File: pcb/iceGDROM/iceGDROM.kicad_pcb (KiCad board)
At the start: 2 copper layers, 100 x 40 mm, 128 parts, among them J1 Micro_SD_Card_Det_Hirose_DM3AT, J2 Conn_02x22_Odd_Even, J3 Conn_02x04_Odd_Even, SW1 SW_Push, SW2 SW_Push, SW3 SW_Push, U1 ICE40HX8K-BG121, U2 LD1117S12TR_SOT223, U3 ME6206A25M3G_SOT23, U4 W25Q32JVSS, X1 SG-310SCF

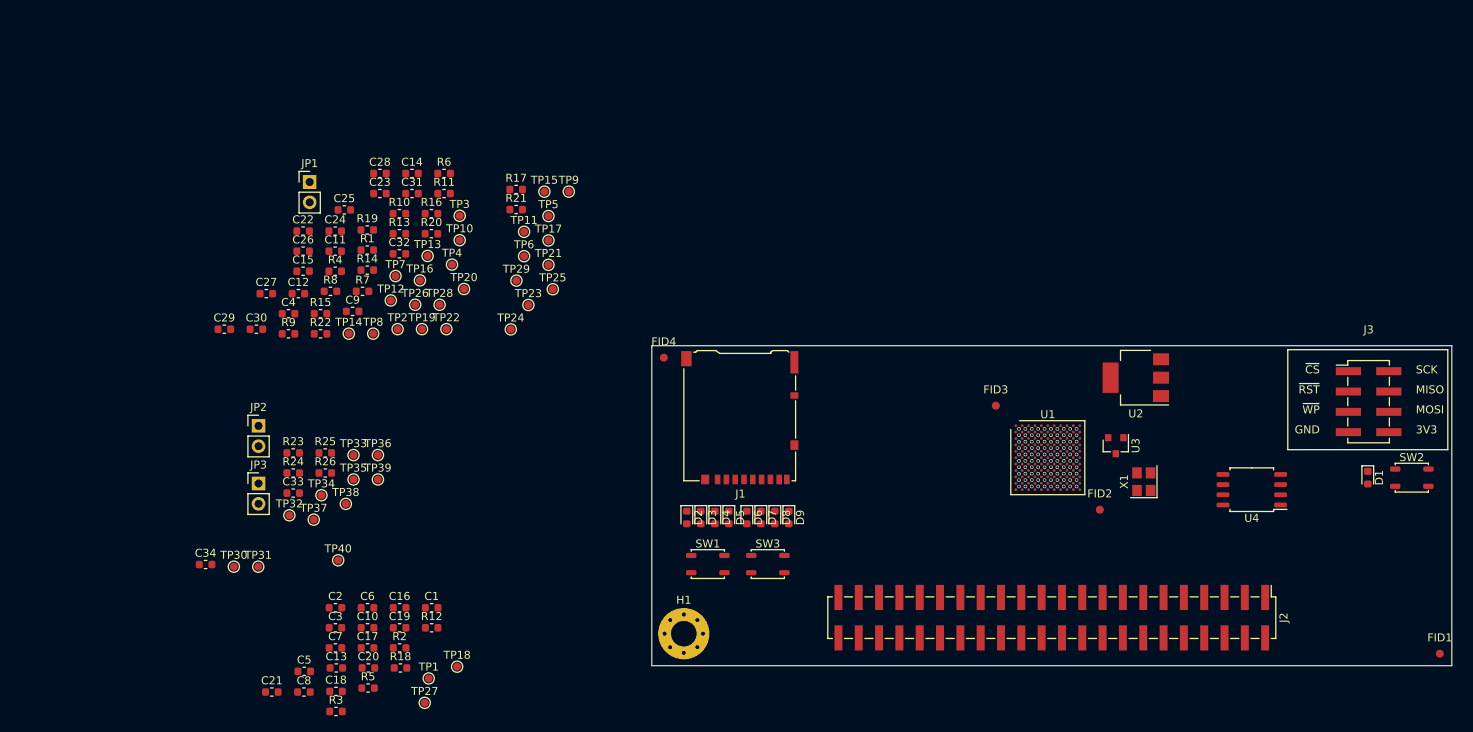
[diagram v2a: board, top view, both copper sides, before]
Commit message: Completed a functional version of the schematic and started with basic layout of the components on the PCB.
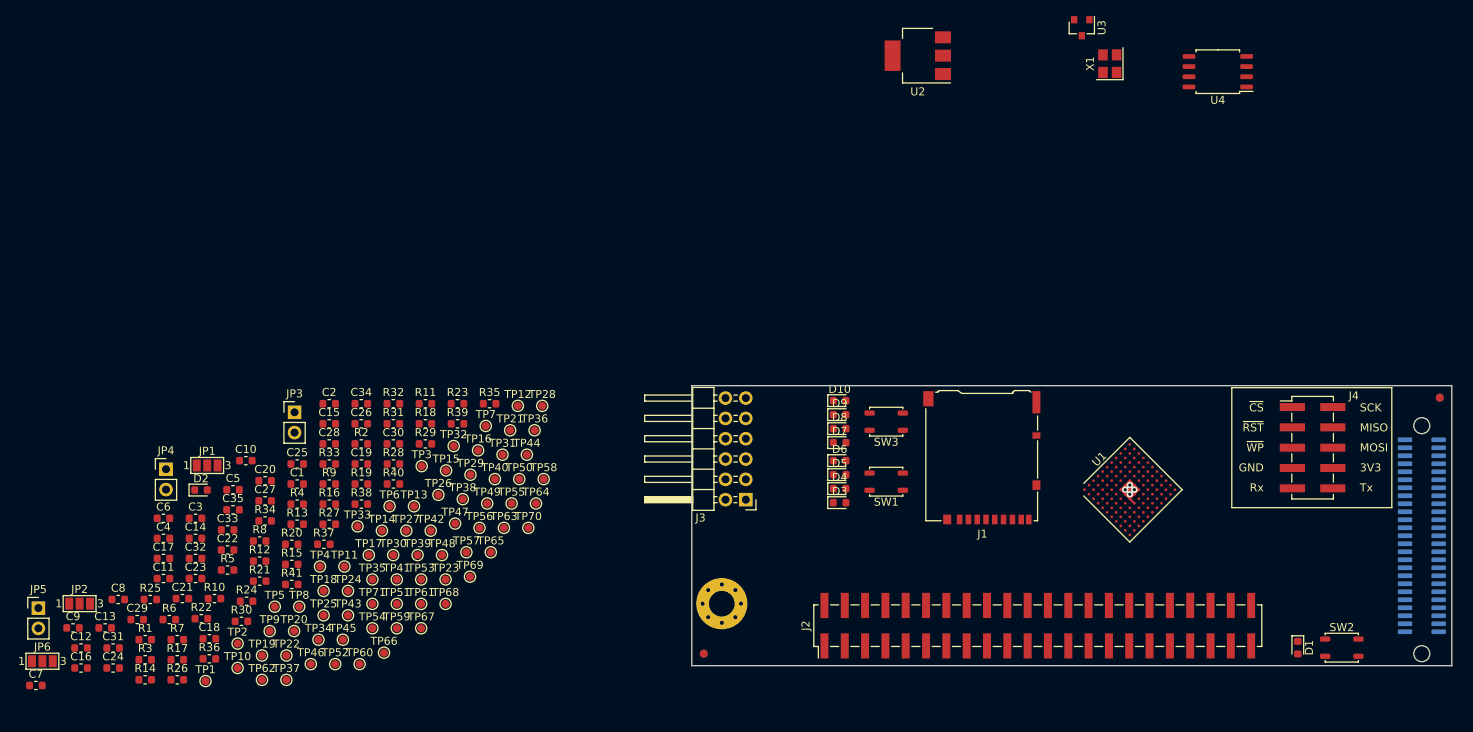
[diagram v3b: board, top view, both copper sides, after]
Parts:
- added C35: 10u, Capacitor_SMD:C_0603_1608Metric, F.Cu at (62.7, 85.5)
- added CN1: Molex_52602_0579, iceGDROM:Molex_052602_0579, B.Cu at (211.2, 89.2)
- added D2: LED, LED_SMD:LED_0603_1608Metric, F.Cu at (58.6, 83.0)
- added J4: Conn_02x05_Odd_Even, Connector_PinHeader_2.54mm:PinHeader_2x05_P2.54mm_Vertical_SMD, F.Cu at (197.6, 77.8)
- added JP4: Jumper_NC_Small, Connector_PinHeader_2.54mm:PinHeader_1x02_P2.54mm_Vertical, F.Cu at (54.3, 80.4)
- added JP5: Jumper_NC_Small, Connector_PinHeader_2.54mm:PinHeader_1x02_P2.54mm_Vertical, F.Cu at (38.3, 97.8)
- added JP6: Jumper_NC_Dual, Jumper:SolderJumper-3_P1.3mm_Open_Pad1.0x1.5mm_NumberLabels, F.Cu at (38.8, 104.4)
- added R27: 10K, Resistor_SMD:R_0603_1608Metric, F.Cu at (74.7, 87.3)
- added R28: 10K, Resistor_SMD:R_0603_1608Metric, F.Cu at (82.7, 79.8)
- added R29: 10K, Resistor_SMD:R_0603_1608Metric, F.Cu at (86.7, 77.3)
- added R30: 10K, Resistor_SMD:R_0603_1608Metric, F.Cu at (63.7, 99.5)
- added R31: 10K, Resistor_SMD:R_0603_1608Metric, F.Cu at (82.7, 74.8)
- added R32: 10K, Resistor_SMD:R_0603_1608Metric, F.Cu at (82.7, 72.3)
- added R33: 10K, Resistor_SMD:R_0603_1608Metric, F.Cu at (74.7, 79.8)
- added R34: 10K, Resistor_SMD:R_0603_1608Metric, F.Cu at (66.7, 86.9)
- added R35: 10K, Resistor_SMD:R_0603_1608Metric, F.Cu at (94.7, 72.3)
- added R36: NP, Resistor_SMD:R_0603_1608Metric, F.Cu at (59.7, 104.1)
- added R37: NP, Resistor_SMD:R_0603_1608Metric, F.Cu at (74.0, 89.8)
- added R38: 10K, Resistor_SMD:R_0603_1608Metric, F.Cu at (78.7, 84.8)
- added R39: 10K, Resistor_SMD:R_0603_1608Metric, F.Cu at (90.7, 74.8)
- added R40: 100R, Resistor_SMD:R_0603_1608Metric, F.Cu at (82.7, 82.3)
- added R41: 100R, Resistor_SMD:R_0603_1608Metric, F.Cu at (70.0, 94.8)
- added TP41: TestPoint_Probe, TestPoint:TestPoint_Pad_D1.0mm, F.Cu at (83.1, 94.2)
- added TP42: TestPoint_Probe, TestPoint:TestPoint_Pad_D1.0mm, F.Cu at (87.4, 88.1)
- added TP43: TestPoint_Probe, TestPoint:TestPoint_Pad_D1.0mm, F.Cu at (77.0, 98.7)
- added TP44: TestPoint_Probe, TestPoint:TestPoint_Pad_D1.0mm, F.Cu at (99.4, 78.6)
- added TP45: TestPoint_Probe, TestPoint:TestPoint_Pad_D1.0mm, F.Cu at (76.4, 101.8)
- added TP46: TestPoint_Probe, TestPoint:TestPoint_Pad_D1.0mm, F.Cu at (72.4, 104.8)
- added TP47: TestPoint_Probe, TestPoint:TestPoint_Pad_D1.0mm, F.Cu at (90.4, 87.2)
- added TP48: TestPoint_Probe, TestPoint:TestPoint_Pad_D1.0mm, F.Cu at (88.8, 91.2)
- added TP49: TestPoint_Probe, TestPoint:TestPoint_Pad_D1.0mm, F.Cu at (94.4, 84.7)
- added TP50: TestPoint_Probe, TestPoint:TestPoint_Pad_D1.0mm, F.Cu at (98.4, 81.7)
- added TP51: TestPoint_Probe, TestPoint:TestPoint_Pad_D1.0mm, F.Cu at (83.1, 97.3)
- added TP52: TestPoint_Probe, TestPoint:TestPoint_Pad_D1.0mm, F.Cu at (75.4, 104.8)
- added TP53: TestPoint_Probe, TestPoint:TestPoint_Pad_D1.0mm, F.Cu at (86.2, 94.2)
- added TP54: TestPoint_Probe, TestPoint:TestPoint_Pad_D1.0mm, F.Cu at (80.1, 100.3)
- added TP55: TestPoint_Probe, TestPoint:TestPoint_Pad_D1.0mm, F.Cu at (97.5, 84.7)
- added TP56: TestPoint_Probe, TestPoint:TestPoint_Pad_D1.0mm, F.Cu at (93.5, 87.8)
- added TP57: TestPoint_Probe, TestPoint:TestPoint_Pad_D1.0mm, F.Cu at (91.8, 90.8)
- added TP58: TestPoint_Probe, TestPoint:TestPoint_Pad_D1.0mm, F.Cu at (101.5, 81.7)
- added TP59: TestPoint_Probe, TestPoint:TestPoint_Pad_D1.0mm, F.Cu at (83.1, 100.3)
- added TP60: TestPoint_Probe, TestPoint:TestPoint_Pad_D1.0mm, F.Cu at (78.5, 104.8)
- added TP61: TestPoint_Probe, TestPoint:TestPoint_Pad_D1.0mm, F.Cu at (86.2, 97.3)
- added TP62: TestPoint_Probe, TestPoint:TestPoint_Pad_D1.0mm, F.Cu at (66.3, 106.8)
- added TP63: TestPoint_Probe, TestPoint:TestPoint_Pad_D1.0mm, F.Cu at (96.5, 87.8)
- added TP64: TestPoint, TestPoint:TestPoint_Pad_D1.0mm, F.Cu at (100.5, 84.7)
- added TP65: TestPoint, TestPoint:TestPoint_Pad_D1.0mm, F.Cu at (94.9, 90.8)
- added TP66: TestPoint, TestPoint:TestPoint_Pad_D1.0mm, F.Cu at (81.5, 103.4)
- added TP67: TestPoint, TestPoint:TestPoint_Pad_D1.0mm, F.Cu at (86.2, 100.3)
- added TP68: TestPoint, TestPoint:TestPoint_Pad_D1.0mm, F.Cu at (89.2, 97.3)
- added TP69: TestPoint, TestPoint:TestPoint_Pad_D1.0mm, F.Cu at (92.3, 93.9)
- added TP70: TestPoint, TestPoint:TestPoint_Pad_D1.0mm, F.Cu at (99.6, 87.8)
- added TP71: TestPoint, TestPoint:TestPoint_Pad_D1.0mm, F.Cu at (80.1, 97.3)
- C21: value 10n -> NP
- C22: value 100n -> 10n
- C30, C8: value 10u -> 100n
- C32, C9: value 100n -> 10u
- C33: value 1u0 -> 100n
- C34: value 10u -> 1u0
- FID3, FID4: moved to B.Cu
- J3: value Conn_02x04_Odd_Even -> PMOD; footprint Connector_PinHeader_2.54mm:PinHeader_2x04_P2.54mm_Vertical_SMD -> Connector_PinHeader_2.54mm:PinHeader_2x06_P2.54mm_Horizontal
- JP1, JP2: value Jumper_NC_Small -> Jumper_NC_Dual; footprint Connector_PinHeader_2.54mm:PinHeader_1x02_P2.54mm_Vertical -> Jumper:SolderJumper-3_P1.3mm_Open_Pad1.0x1.5mm_NumberLabels
- R10, R11: value 10K -> 1K
- R2: value R -> 100R
- R21, R22: value NP -> 10K
- R25, R26: value 100R -> 10K
- R3: value 1K -> 10K
- R4, R5, R6, R7: value 10K -> 100R
- R9: value 10K -> R
- TP1, TP10, TP11, TP12, TP13, TP14, TP15, TP16, TP17, TP18, TP19, TP2, TP20, TP21, TP22, TP23, TP24, TP25, TP26, TP27, TP28, TP29, TP3, TP30, TP31, TP36, TP37, TP38, TP39, TP4, TP5, TP6, TP7, TP8, TP9: value TestPoint -> TestPoint_Probe
- moved J3 78.8 mm to (126.8, 84.2), turned to 180 degrees
- moved R17 72.5 mm to (55.7, 104.3)
- moved C31 68.0 mm to (47.7, 102.8)
- moved TP9 66.4 mm to (67.2, 100.7)
- moved R6 65.5 mm to (54.7, 99.2)
- moved C24 61.3 mm to (47.7, 105.3)
- moved TP10 60.2 mm to (63.2, 105.3)
- moved TP5 59.6 mm to (67.9, 97.6)
- moved R14 58.3 mm to (51.7, 106.8)
- moved R21 56.4 mm to (66.0, 94.4)
- moved R1 56.1 mm to (51.7, 101.7)
- moved FID3 55.5 mm to (213.5, 71.5)
- moved R10 53.4 mm to (60.3, 96.6)
- moved C23 53.4 mm to (58.0, 94.1)
- moved C14 53.0 mm to (58.0, 89.1)
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- renumbered D9 to D10, D2 to D3, D3 to D4, D4 to D5, D5 to D6, D6 to D7, D7 to D8, D8 to D9
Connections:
- C10 pad 1: GND -> +3V3
- C10 pad 2: +3V3 -> GND
- C11 pad 1: +3V3 -> GND
- C11 pad 2: GND -> +3V3
- C12 pad 1: +3V3 -> GND
- C12 pad 2: GND -> +3V3
- C18 pad 1: Net-(C18-Pad1) -> /ROM_UP
- C21 pad 1: Net-(C21-Pad1) -> +3V3
- C22 pad 1: +3V3 -> /ROM_DWN
- C24 pad 1: +2V5 -> +3V3
- C25 pad 1: +1V2 -> +2V5
- C27 pad 1: Net-(C27-Pad1) -> +1V2
- C27 pad 2: Net-(C27-Pad2) -> GND
- C29 pad 1: +1V2 -> Net-(C29-Pad1)
- C29 pad 2: GND -> Net-(C29-Pad2)
- C30 pad 1: Net-(C27-Pad1) -> +1V2
- C30 pad 2: Net-(C27-Pad2) -> GND
- C32 pad 1: +1V2 -> Net-(C29-Pad1)
- C32 pad 2: GND -> Net-(C29-Pad2)
- C8 pad 1: GND -> +3V3
- C8 pad 2: +3V3 -> GND
- D10 pad 2: Net-(D9-Pad2) -> Net-(D10-Pad2)
- D3 pad 2: Net-(D2-Pad2) -> Net-(D3-Pad2)
- D4 pad 2: Net-(D3-Pad2) -> Net-(D4-Pad2)
- D5 pad 2: Net-(D4-Pad2) -> Net-(D5-Pad2)
- D6 pad 2: Net-(D5-Pad2) -> Net-(D6-Pad2)
- D7 pad 2: Net-(D6-Pad2) -> Net-(D7-Pad2)
- D8 pad 2: Net-(D7-Pad2) -> Net-(D8-Pad2)
- D9 pad 2: Net-(D8-Pad2) -> Net-(D9-Pad2)
- J3 pad 1: /FLASH_CSn -> Net-(J3-Pad1)
- J3 pad 2: /FPGA_SCK -> Net-(J3-Pad2)
- J3 pad 3: /FLASH_~RST~|IO3 -> Net-(J3-Pad3)
- J3 pad 4: /FLASH_MISO|IO1 -> Net-(J3-Pad4)
- J3 pad 5: /FLASH_~WP~|IO2 -> GND
- J3 pad 6: /FLASH_MOSI|IO0 -> +3V3
- J3 pad 7: GND -> Net-(J3-Pad7)
- J3 pad 8: +3V3 -> Net-(J3-Pad8)
- JP1 pad 1: /FLASH_CSn -> GND
- JP1 pad 2: Net-(JP1-Pad2) -> /CSEL
- JP2 pad 1: /FLASH_MOSI|IO0 -> +3V3
- JP2 pad 2: /FPGA_SDO -> /VLOGIC
- JP3 pad 1: /FPGA_SDI -> /FLASH_CSn
- JP3 pad 2: /FLASH_MISO|IO1 -> Net-(JP3-Pad2)
- R10 pad 1: Net-(D4-Pad2) -> Net-(R10-Pad1)
- R10 pad 2: /LED2 -> Net-(D1-Pad2)
- R11 pad 1: Net-(D5-Pad2) -> Net-(D2-Pad2)
- R11 pad 2: /LED3 -> +3V3
- R12 pad 1: Net-(C18-Pad1) -> GND
- R13 pad 1: GND -> Net-(J3-Pad1)
- R13 pad 2: Net-(R13-Pad2) -> /PMOD_1
- R14 pad 1: Net-(D6-Pad2) -> Net-(J3-Pad2)
- R14 pad 2: /LED4 -> /PMOD_2
- R15 pad 1: Net-(D7-Pad2) -> Net-(J3-Pad3)
- R15 pad 2: /LED5 -> /PMOD_3
- R16 pad 1: Net-(D8-Pad2) -> Net-(J3-Pad4)
- R16 pad 2: /LED6 -> /PMOD_4
- R17 pad 1: Net-(D9-Pad2) -> Net-(D3-Pad2)
- R17 pad 2: /LED7 -> /LED0
- R18 pad 1: Net-(C21-Pad1) -> Net-(D4-Pad2)
- R18 pad 2: Net-(R13-Pad2) -> /LED1
- R19 pad 1: +3V3 -> Net-(D5-Pad2)
- R19 pad 2: /FPGA_SCK -> /LED2
- R2 pad 1: Net-(R2-Pad1) -> /EMPH
- R2 pad 2: +3V3 -> /PB0
- R20 pad 1: +3V3 -> Net-(D6-Pad2)
- R20 pad 2: Net-(JP1-Pad2) -> /LED3
- R21 pad 1: +3V3 -> /ROM_UP
- R21 pad 2: /FLASH_MOSI|IO0 -> Net-(R12-Pad2)
- R22 pad 1: +3V3 -> Net-(C16-Pad2)
- R22 pad 2: /FLASH_MISO|IO1 -> Net-(R22-Pad2)
- R23 pad 1: +3V3 -> Net-(R22-Pad2)
- R23 pad 2: /FLASH_~WP~|IO2 -> +3V3
- R24 pad 1: +3V3 -> GND
- R24 pad 2: /FLASH_~RST~|IO3 -> Net-(R24-Pad2)
- R25 pad 1: +1V2 -> /PMOD_5
- R25 pad 2: Net-(C27-Pad1) -> Net-(J3-Pad7)
- R26 pad 1: +1V2 -> /PMOD_6
- R26 pad 2: Net-(C28-Pad1) -> Net-(J3-Pad8)
- R3 pad 1: Net-(R2-Pad1) -> GND
- R3 pad 2: Net-(D1-Pad2) -> /EMPH
- R4 pad 2: +3V3 -> /SDAT
- R5 pad 1: Net-(C16-Pad2) -> Net-(R5-Pad1)
- R5 pad 2: Net-(R5-Pad2) -> /SCK
- R6 pad 1: GND -> Net-(R6-Pad1)
- R6 pad 2: Net-(R12-Pad2) -> /CD_CLK
- R7 pad 1: Net-(R5-Pad2) -> Net-(R7-Pad1)
- R7 pad 2: +3V3 -> /LRCK
- R8 pad 1: Net-(D2-Pad2) -> Net-(R8-Pad1)
- R8 pad 2: /LED0 -> +3V3
- R9 pad 1: Net-(D3-Pad2) -> Net-(R10-Pad1)
- R9 pad 2: /LED1 -> +3V3
- SW2 pad 1: Net-(R5-Pad2) -> Net-(R22-Pad2)
- SW3 pad 2: Net-(R13-Pad2) -> Net-(R24-Pad2)
- TP1 pad 1: Net-(R2-Pad1) -> /PB0
- TP10 pad 1: /D8 -> /ROM_DWN
- TP11 pad 1: /D9 -> /LED0
- TP12 pad 1: /D10 -> /REFCLK
- TP13 pad 1: /D11 -> /LED1
- TP14 pad 1: /D12 -> /LED2
- TP15 pad 1: /D13 -> /LED3
- TP16 pad 1: /D14 -> /LED4
- TP17 pad 1: /D15 -> /LED5
- TP18 pad 1: /REFCLK -> /LED6
- TP19 pad 1: /PB0 -> /LED7
- TP2 pad 1: /D0 -> /PB1
- TP20 pad 1: /PB1 -> /UART_Tx
- TP21 pad 1: /PB2 -> /UART_Rx
- TP22 pad 1: /PB3 -> /EMPH
- TP23 pad 1: /PB4 -> /CS0n
- TP24 pad 1: /PB5 -> /CS1n
- TP25 pad 1: /PB6 -> /RDn
- TP26 pad 1: /PB7 -> /WRn
- TP27 pad 1: Net-(C16-Pad2) -> /DMACKn
- TP28 pad 1: +12V -> /DMARQ
- TP29 pad 1: +5V -> /IORDY
- TP3 pad 1: /D1 -> /PB2
- TP30 pad 1: +3V3 -> /INTRQ
- TP31 pad 1: +2V5 -> /G_RST
- TP32 pad 1: +1V2 -> Net-(R10-Pad1)
- TP33 pad 1: Net-(JP1-Pad2) -> /REFCLK
- TP34 pad 1: /FPGA_SCK -> +1V2
- TP35 pad 1: Net-(C27-Pad1) -> +2V5
- TP36 pad 1: Net-(C28-Pad1) -> /PMOD_1
- TP37 pad 1: /FLASH_MOSI|IO0 -> /PMOD_2
- TP38 pad 1: /FLASH_MISO|IO1 -> /PMOD_3
- TP39 pad 1: /FLASH_~WP~|IO2 -> /PMOD_4
- TP4 pad 1: /D2 -> /PB3
- TP40 pad 1: /FLASH_~RST~|IO3 -> Net-(C16-Pad2)
- TP5 pad 1: /D3 -> /PB4
- TP6 pad 1: /D4 -> /PB5
- TP7 pad 1: /D5 -> /PB6
- TP8 pad 1: /D6 -> /PB7
- TP9 pad 1: /D7 -> /ROM_UP
- U1 pad A10: Net-(U1-PadA10) -> /PB1
- U1 pad A11: Net-(U1-PadA11) -> /PB0
- U1 pad A2: Net-(U1-PadA2) -> /UART_Tx
- U1 pad A3: Net-(U1-PadA3) -> /UART_Rx
- U1 pad A4: Net-(U1-PadA4) -> /LED4
- U1 pad A5: Net-(U1-PadA5) -> /LED2
- U1 pad A6: Net-(U1-PadA6) -> /LED1
- U1 pad A7: Net-(U1-PadA7) -> /LED0
- U1 pad A8: Net-(U1-PadA8) -> /ROM_UP
- U1 pad A9: Net-(U1-PadA9) -> /PB5
- U1 pad B1: Net-(U1-PadB1) -> /D0
- U1 pad B2: Net-(U1-PadB2) -> /D1
- U1 pad B3: Net-(U1-PadB3) -> /LED7
- U1 pad B4: Net-(U1-PadB4) -> /LED6
- U1 pad B5: Net-(U1-PadB5) -> /LED3
- U1 pad B6: Net-(U1-PadB6) -> /REFCLK
- U1 pad B8: Net-(U1-PadB8) -> /PB4
- U1 pad B9: Net-(U1-PadB9) -> /PB3
- U1 pad C1: Net-(U1-PadC1) -> /D5
- U1 pad C2: Net-(U1-PadC2) -> /D4
- U1 pad C3: Net-(U1-PadC3) -> /D3
- U1 pad C4: Net-(U1-PadC4) -> /D2
- U1 pad C5: Net-(C28-Pad2) -> Net-(C29-Pad2)
- U1 pad C6: Net-(C28-Pad1) -> Net-(C29-Pad1)
- U1 pad C7: Net-(U1-PadC7) -> /ROM_DWN
- U1 pad C8: Net-(U1-PadC8) -> /PB6
- U1 pad C9: Net-(U1-PadC9) -> /PB2
- U1 pad D1: Net-(U1-PadD1) -> /D7
- U1 pad D2: Net-(U1-PadD2) -> /D8
- U1 pad D3: Net-(U1-PadD3) -> /D9
- U1 pad D5: Net-(U1-PadD5) -> /LED5
- U1 pad D7: Net-(U1-PadD7) -> /PB7
- U1 pad E1: Net-(U1-PadE1) -> /D6
- U1 pad E2: Net-(U1-PadE2) -> /D10
- U1 pad E3: Net-(U1-PadE3) -> /D11
- U1 pad E8: Net-(U1-PadE8) -> Net-(R7-Pad1)
- U1 pad E9: Net-(U1-PadE9) -> Net-(R6-Pad1)
- U1 pad F1: Net-(U1-PadF1) -> /D12
- U1 pad F10: Net-(U1-PadF10) -> Net-(R4-Pad1)
- U1 pad F2: Net-(U1-PadF2) -> /D13
- U1 pad F4: Net-(U1-PadF4) -> /D14
- U1 pad F9: Net-(U1-PadF9) -> Net-(R5-Pad1)
- U1 pad G10: Net-(U1-PadG10) -> /IORDY
- U1 pad G11: Net-(U1-PadG11) -> /G_RST
- U1 pad G2: Net-(U1-PadG2) -> /D15
- U1 pad G3: Net-(U1-PadG3) -> /A0
- U1 pad G8: Net-(U1-PadG8) -> /DMACKn
- U1 pad G9: Net-(U1-PadG9) -> /INTRQ
- U1 pad H1: Net-(U1-PadH1) -> /A2
- U1 pad H10: Net-(U1-PadH10) -> /RDn
- U1 pad H11: Net-(U1-PadH11) -> /DMARQ
- U1 pad H3: Net-(U1-PadH3) -> /A1
- U1 pad J10: Net-(U1-PadJ10) -> /WRn
- U1 pad J11: Net-(U1-PadJ11) -> /CS0n
- U1 pad J3: Net-(U1-PadJ3) -> /PMOD_2
- U1 pad J4: Net-(U1-PadJ4) -> /PMOD_5
- U1 pad J6: Net-(C27-Pad1) -> Net-(C28-Pad1)
- U1 pad K11: Net-(U1-PadK11) -> /CS1n
- U1 pad K3: Net-(U1-PadK3) -> /PMOD_4
- U1 pad K4: Net-(U1-PadK4) -> /PMOD_8
- U1 pad K8: Net-(R2-Pad1) -> Net-(R10-Pad1)
- U1 pad L1: Net-(U1-PadL1) -> /PMOD_1
- U1 pad L2: Net-(U1-PadL2) -> /PMOD_3
- U1 pad L3: Net-(U1-PadL3) -> /PMOD_6
- U1 pad L4: Net-(U1-PadL4) -> /PMOD_7
- U1 pad L6: Net-(C27-Pad2) -> Net-(C28-Pad2)
- U4 pad 1: Net-(JP1-Pad2) -> Net-(JP3-Pad2)
- X1 pad 1: Net-(R4-Pad1) -> Net-(R8-Pad1)
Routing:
- net GND: track 0.00 -> 10.4 mm, vias 0 -> 1
- net (no net): vias 100 -> 3
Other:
- board size 100 x 40 mm -> 95 x 35 mm
- copper layers 2 -> 4
- board text added: "Rx"
- board text added: "Tx"

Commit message: Split the IDE header into 40+4 due to SMD header availability. Started with layout of the PCB.
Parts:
- added J3: Conn_02x02_Odd_Even, Connector_PinSocket_2.54mm:PinSocket_2x02_P2.54mm_Vertical_SMD, F.Cu at (134.0, 100.0)
- C26, C27, C30, C33, C34, C35: moved to B.Cu
- H1: value MountingHole -> MountingHole_Pad
- J2: value Conn_02x22_Odd_Even -> Conn_02x20_Odd_Even; footprint Connector_PinHeader_2.54mm:PinHeader_2x22_P2.54mm_Vertical_SMD -> Connector_PinSocket_2.54mm:PinSocket_2x20_P2.54mm_Vertical_SMD
- moved C35 122.4 mm to (184.6, 74.8), turned to 270 degrees
- moved C27 111.8 mm to (178.4, 80.8), turned to 315 degrees
- moved C33 111.2 mm to (172.2, 73.3), turned to 315 degrees
- moved C34 105.2 mm to (183.8, 76.7)
- moved C15 105.0 mm to (179.7, 75.3), turned to 135 degrees
- moved C26 100.5 mm to (178.7, 84.1), turned to 225 degrees
- moved C30 90.9 mm to (173.4, 71.9), turned to 315 degrees
- moved U3 49.7 mm to (181.5, 73.2), turned to 45 degrees
- moved J2 3.75 mm to (167.0, 100.0), turned to 270 degrees
- moved U1 2.80 mm to (177.5, 82.5)
- moved J5 2.00 mm to (199.6, 77.8)
- moved H1 0.50 mm to (123.8, 97.8)
- renumbered J3 to J4, J4 to J5
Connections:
- CN1 pad 27: Net-(CN1-Pad27) -> (no net)
- H1 pad 1: (no net) -> GND
- J2 pad 20: Net-(J2-Pad20) -> (no net)
- J2 pad 32: Net-(J2-Pad32) -> (no net)
- J2 pad 34: Net-(J2-Pad34) -> (no net)
- JP1 pad 3: Net-(JP1-Pad3) -> (no net)
- U1 pad A1: Net-(U1-PadA1) -> (no net)
- U1 pad B10: Net-(U1-PadB10) -> (no net)
- U1 pad B11: Net-(U1-PadB11) -> (no net)
- U1 pad B7: Net-(U1-PadB7) -> (no net)
- U1 pad C11: Net-(U1-PadC11) -> (no net)
- U1 pad D10: Net-(U1-PadD10) -> (no net)
- U1 pad D11: Net-(U1-PadD11) -> (no net)
- U1 pad D9: Net-(U1-PadD9) -> (no net)
- U1 pad E10: Net-(U1-PadE10) -> (no net)
- U1 pad E11: Net-(U1-PadE11) -> (no net)
- U1 pad F11: Net-(U1-PadF11) -> (no net)
- U1 pad F3: Net-(U1-PadF3) -> (no net)
- U1 pad G1: Net-(U1-PadG1) -> (no net)
- U1 pad H2: Net-(U1-PadH2) -> (no net)
- U1 pad H7: Net-(U1-PadH7) -> (no net)
- U1 pad H9: Net-(U1-PadH9) -> (no net)
- U1 pad J1: Net-(U1-PadJ1) -> (no net)
- U1 pad J2: Net-(U1-PadJ2) -> (no net)
- U1 pad J5: Net-(U1-PadJ5) -> (no net)
- U1 pad J7: Net-(U1-PadJ7) -> (no net)
- U1 pad J8: Net-(U1-PadJ8) -> (no net)
- U1 pad K1: Net-(U1-PadK1) -> (no net)
- U1 pad K2: Net-(U1-PadK2) -> (no net)
- U1 pad K5: Net-(U1-PadK5) -> (no net)
- U1 pad K6: Net-(U1-PadK6) -> (no net)
- U1 pad K7: Net-(U1-PadK7) -> (no net)
- U1 pad L5: Net-(U1-PadL5) -> (no net)
- U1 pad L7: Net-(U1-PadL7) -> (no net)
- U1 pad L8: Net-(U1-PadL8) -> (no net)
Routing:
- net +2V5: track 0.00 -> 7.41 mm
- net +1V2: track 0.00 -> 3.23 mm, vias 0 -> 4
- net GND: track 10.4 -> 8.69 mm, vias 1 -> 11
- net (no net): vias 3 -> 0
- added copper zone on B.Cu, net GND
- added copper zone on In1.Cu, net GND
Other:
- board text added: "A1"

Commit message: Completed functionality of the PCB layout. Still have to do the silkscreen though.
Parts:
- removed C11, C17, C5: 10u, Capacitor_SMD:C_0603_1608Metric
- removed C12, C19, C2, C6: 1u0, Capacitor_SMD:C_0603_1608Metric
- removed R13, R14, R15, R16, R17, R18, R19, R20, R25, R26, R27, R28, R29, R30, R31, R32, R34, R35, R38, R39: 10K, Resistor_SMD:R_0603_1608Metric
- removed R4, R5, R6, R7: 100R, Resistor_SMD:R_0603_1608Metric
- removed TP1, TP19, TP20, TP21, TP22, TP23, TP24, TP25, TP26, TP27, TP28, TP29, TP30, TP31, TP45, TP46, TP47, TP48, TP49, TP50, TP51, TP52, TP53, TP54, TP55, TP56, TP57, TP58, TP59, TP60, TP61, TP62, TP63: TestPoint_Probe, TestPoint:TestPoint_Pad_D1.0mm
- removed TP32, TP40, TP64, TP65, TP66, TP67, TP68, TP69, TP70, TP71: TestPoint, TestPoint:TestPoint_Pad_D1.0mm
- added REF**: Symbol_GNU-Logo_SilkscreenTop, Symbol:Symbol_GNU-Logo_SilkscreenTop, B.Cu at (154.5, 89.0)
- added REF**: OSHW-Logo2_14.6x12mm_SilkScreen, Symbol:OSHW-Logo2_14.6x12mm_SilkScreen, B.Cu at (139.0, 90.5)
- added RN1: 10K, Resistor_SMD:R_Array_Convex_4x0603, F.Cu at (142.8, 85.7)
- added RN2: R_Pack04, Resistor_SMD:R_Array_Convex_4x0603, F.Cu at (142.3, 80.6)
- added RN3: 10K, Resistor_SMD:R_Array_Convex_4x0603, F.Cu at (142.8, 89.9)
- added RN4: R_Pack04, Resistor_SMD:R_Array_Convex_4x0603, F.Cu at (135.5, 80.5)
- added RN5: 10K, Resistor_SMD:R_Array_Convex_4x0603, F.Cu at (188.6, 89.2)
- added RN6: 100R, Resistor_SMD:R_Array_Convex_4x0603, B.Cu at (203.2, 79.8)
- C1: value 10u -> 100n; moved to B.Cu
- C13, C20, C23, C25, C28, C29, C3, C31, C32, C7, R10, R2, R3, R40, R41, R9: moved to B.Cu
- C34, C35: moved to F.Cu
- J4: footprint Connector_PinHeader_2.54mm:PinHeader_2x06_P2.54mm_Horizontal -> iceGDROM:PMOD_Host_2x06_P2.54mm_Horizontal
- JP1: footprint Jumper:SolderJumper-3_P1.3mm_Open_Pad1.0x1.5mm_NumberLabels -> Jumper:SolderJumper-3_P1.3mm_Bridged12_RoundedPad1.0x1.5mm; moved to B.Cu
- JP2, JP6: value Jumper_NC_Dual -> Jumper_3_Bridged12; footprint Jumper:SolderJumper-3_P1.3mm_Open_Pad1.0x1.5mm_NumberLabels -> Jumper:SolderJumper-3_P1.3mm_Bridged12_RoundedPad1.0x1.5mm_NumberLabels
- JP3: value Jumper_NC_Small -> SolderJumper_2_Bridged; footprint Connector_PinHeader_2.54mm:PinHeader_1x02_P2.54mm_Vertical -> Jumper:SolderJumper-2_P1.3mm_Open_TrianglePad1.0x1.5mm; moved to B.Cu
- JP4, JP5: footprint Connector_PinHeader_2.54mm:PinHeader_1x02_P2.54mm_Vertical -> Jumper:SolderJumper-2_P1.3mm_Bridged_Pad1.0x1.5mm; moved to B.Cu
- moved JP5 168.3 mm to (204.8, 73.6), turned to 90 degrees
- moved C9 161.5 mm to (204.1, 95.7), turned to 180 degrees
- moved R3 151.8 mm to (202.3, 85.2), turned to 180 degrees
- moved C16 151.2 mm to (194.8, 101.4), turned to 180 degrees
- moved C24 150.3 mm to (197.4, 91.8), turned to 90 degrees
- moved JP4 148.5 mm to (202.7, 73.6), turned to 90 degrees
- moved C14 143.1 mm to (200.8, 98.8)
- moved C7 140.9 mm to (176.0, 78.8), turned to 315 degrees
- moved R22 136.2 mm to (194.8, 103.0)
- moved C13 135.7 mm to (181.6, 86.2), turned to 225 degrees
- moved C31 130.9 mm to (177.6, 87.0), turned to 315 degrees
- moved R36 129.6 mm to (188.7, 92.1)
- moved C8 127.3 mm to (173.3, 72.7), turned to 90 degrees
- moved R10 124.9 mm to (183.3, 74.8), turned to 180 degrees
- moved TP34 124.1 mm to (197.4, 97.3)
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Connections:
- C18 pad 1: /ROM_UP -> /ROM_DWN
- C22 pad 1: /ROM_DWN -> /ROM_UP
- CN1 pad 27: (no net) -> Net-(CN1-Pad27)
- J2 pad 20: (no net) -> Net-(J2-Pad20)
- J2 pad 32: (no net) -> Net-(J2-Pad32)
- J2 pad 34: (no net) -> Net-(J2-Pad34)
- J3 pad 4: (no net) -> Net-(J3-Pad4)
- JP1 pad 3: (no net) -> Net-(JP1-Pad3)
- R21 pad 1: /ROM_UP -> /ROM_DWN
- R33 pad 1: /ROM_DWN -> /ROM_UP
- TP11 pad 1: /LED0 -> Net-(D3-Pad2)
- TP12 pad 1: /REFCLK -> Net-(D4-Pad2)
- TP13 pad 1: /LED1 -> Net-(D5-Pad2)
- TP14 pad 1: /LED2 -> Net-(D6-Pad2)
- TP15 pad 1: /LED3 -> Net-(D7-Pad2)
- TP16 pad 1: /LED4 -> Net-(D8-Pad2)
- TP17 pad 1: /LED5 -> Net-(D9-Pad2)
- TP18 pad 1: /LED6 -> Net-(D10-Pad2)
- TP36 pad 1: /PMOD_1 -> Net-(J4-Pad1)
- TP37 pad 1: /PMOD_2 -> Net-(J4-Pad2)
- TP38 pad 1: /PMOD_3 -> Net-(J4-Pad3)
- TP39 pad 1: /PMOD_4 -> Net-(J4-Pad4)
- TP41 pad 1: /PMOD_5 -> Net-(J4-Pad7)
- TP42 pad 1: /PMOD_6 -> Net-(J4-Pad8)
- TP43 pad 1: /PMOD_7 -> Net-(J4-Pad9)
- TP44 pad 1: /PMOD_8 -> Net-(J4-Pad10)
- U1 pad A1: (no net) -> /ROM_UP
- U1 pad A10: /PB1 -> /LED2
- U1 pad A11: /PB0 -> /LED0
- U1 pad A2: /UART_Tx -> /PB3
- U1 pad A3: /UART_Rx -> /PB2
- U1 pad A4: /LED4 -> /PB5
- U1 pad A5: /LED2 -> /PMOD_4
- U1 pad A6: /LED1 -> /PMOD_3
- U1 pad A7: /LED0 -> /PMOD_2
- U1 pad A8: /ROM_UP -> /PMOD_1
- U1 pad A9: /PB5 -> /LED4
- U1 pad B1: /D0 -> /ROM_DWN
- U1 pad B10: (no net) -> Net-(U1-PadB10)
- U1 pad B11: (no net) -> /LED6
- U1 pad B2: /D1 -> /PB4
- U1 pad B3: /LED7 -> /PB1
- U1 pad B4: /LED6 -> /PB6
- U1 pad B5: /LED3 -> /PMOD_7
- U1 pad B6: /REFCLK -> /PMOD_6
- U1 pad B7: (no net) -> Net-(U1-PadB7)
- U1 pad B8: /PB4 -> /PMOD_5
- U1 pad B9: /PB3 -> /LED3
- U1 pad C1: /D5 -> /CS0n
- U1 pad C11: (no net) -> /LED7
- U1 pad C2: /D4 -> /CS1n
- U1 pad C3: /D3 -> Net-(U1-PadC3)
- U1 pad C4: /D2 -> /PMOD_8
- U1 pad C7: /ROM_DWN -> Net-(U1-PadC7)
- U1 pad C8: /PB6 -> /LED5
- U1 pad C9: /PB2 -> Net-(U1-PadC9)
- U1 pad D1: /D7 -> /A0
- U1 pad D10: (no net) -> /LED1
- U1 pad D11: (no net) -> /PB7
- U1 pad D2: /D8 -> /A2
- U1 pad D3: /D9 -> Net-(U1-PadD3)
- U1 pad D5: /LED5 -> Net-(U1-PadD5)
- U1 pad D7: /PB7 -> Net-(U1-PadD7)
- U1 pad D9: (no net) -> Net-(U1-PadD9)
- U1 pad E1: /D6 -> /INTRQ
- U1 pad E10: (no net) -> Net-(U1-PadE10)
- U1 pad E11: (no net) -> Net-(U1-PadE11)
- U1 pad E2: /D10 -> /A1
- U1 pad E3: /D11 -> Net-(U1-PadE3)
- U1 pad F1: /D12 -> /IO_RDY
- U1 pad F11: (no net) -> /REFCLK
- U1 pad F2: /D13 -> /DMACKn
- U1 pad F3: (no net) -> Net-(U1-PadF3)
- U1 pad F4: /D14 -> Net-(U1-PadF4)
- U1 pad G1: (no net) -> /WRn
- U1 pad G10: /IORDY -> Net-(RN6-Pad6)
- U1 pad G11: /G_RST -> Net-(RN6-Pad7)
- U1 pad G2: /D15 -> /RDn
- U1 pad G3: /A0 -> Net-(U1-PadG3)
- U1 pad G8: /DMACKn -> Net-(U1-PadG8)
- U1 pad G9: /INTRQ -> Net-(U1-PadG9)
- U1 pad H1: /A2 -> /D0
- U1 pad H10: /RDn -> Net-(U1-PadH10)
- U1 pad H11: /DMARQ -> Net-(RN6-Pad5)
- U1 pad H2: (no net) -> /D15
- U1 pad H3: /A1 -> Net-(U1-PadH3)
- U1 pad H7: (no net) -> Net-(U1-PadH7)
- U1 pad H9: (no net) -> Net-(U1-PadH9)
- U1 pad J1: (no net) -> /D1
- U1 pad J10: /WRn -> /UART_Rx
- U1 pad J11: /CS0n -> /UART_Tx
- U1 pad J2: (no net) -> /DMARQ
- U1 pad J3: /PMOD_2 -> Net-(U1-PadJ3)
- U1 pad J4: /PMOD_5 -> Net-(U1-PadJ4)
- U1 pad J5: (no net) -> Net-(U1-PadJ5)
- U1 pad J7: (no net) -> Net-(U1-PadJ7)
- U1 pad J8: (no net) -> Net-(U1-PadJ8)
- U1 pad K1: (no net) -> /D2
- U1 pad K11: /CS1n -> /PB0
- U1 pad K2: (no net) -> /D14
- U1 pad K3: /PMOD_4 -> /D13
- U1 pad K4: /PMOD_8 -> /D11
- U1 pad K5: (no net) -> /D10
- U1 pad K6: (no net) -> /D9
- U1 pad K7: (no net) -> /D8
- U1 pad L1: /PMOD_1 -> /D3
- U1 pad L2: /PMOD_3 -> /D12
- U1 pad L3: /PMOD_6 -> /D4
- U1 pad L4: /PMOD_7 -> /D5
- U1 pad L5: (no net) -> /D6
- U1 pad L7: (no net) -> /D7
- U1 pad L8: (no net) -> /G_RST
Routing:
- net GND: track 8.69 -> 137.6 mm, vias 11 -> 91
- net +3V3: track 0.00 -> 95.3 mm, vias 0 -> 40
- net +5V: track 0.00 -> 90.9 mm, vias 0 -> 1
- net /CS1n: track 0.00 -> 86.9 mm, vias 0 -> 3
- net /CS0n: track 0.00 -> 86.4 mm, vias 0 -> 1
- net /A1: track 0.00 -> 84.2 mm, vias 0 -> 3
- net /A0: track 0.00 -> 82.7 mm, vias 0 -> 1
- net /A2: track 0.00 -> 81.5 mm, vias 0 -> 3
- net /INTRQ: track 0.00 -> 81.4 mm, vias 0 -> 3
- net +1V2: track 3.23 -> 82.1 mm, vias 4 -> 14
- net /IO_RDY: track 0.00 -> 73.1 mm, vias 0 -> 3
- net /DMACKn: track 0.00 -> 72.9 mm, vias 0 -> 1
- net /WRn: track 0.00 -> 67.1 mm, vias 0 -> 3
- net /RDn: track 0.00 -> 66.9 mm, vias 0 -> 1
- net /DMARQ: track 0.00 -> 64.8 mm, vias 0 -> 1
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- added copper zone on F.Cu, net +1V2
- added copper zone on In2.Cu, net +1V2
- added copper zone on B.Cu, net +3V3
- added copper zone on F.Cu, net +3V3
- added copper zone on In2.Cu, net +3V3
- added copper zone on F.Cu, net GND
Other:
- board size 95 x 35 mm -> 100 x 35 mm
- net class Default: clearance 0.0889 -> 0.127; trace_width 0.0889 -> 0.1524; via_dia 0.45 -> 0.5; via_drill 0.3 -> 0.2
- rule pad_to_mask_clearance: 0.051 -> 0.0508
- rule solder_mask_min_width: 0.25 -> 0.254
- rule trace_clearance: 0.0889 -> 0.127
- rule trace_min: 0.0889 -> 0.1524
- rule via_min_drill: 0.3 -> 0.2
- board text added: "5V"
- board text added: "ACTIVE"
- board text added: "CDONE"
- board text added: "CSEL"
- board text added: "NC"
- board text added: "Rev 1.0"
- board text added: "VLOGIC"
- board text added: "VMOTOR"
- board text added: "iCEGDROM"
